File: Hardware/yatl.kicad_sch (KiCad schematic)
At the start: 17 parts

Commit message: Added schematic and update pins definition
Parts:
- removed AD?: 6x1F-H8.5, arduino_Uno_Rev3-02-TH:1X06, symbol arduino_Uno_Rev3-02-TH-eagle-import:PINHD-1X6
- removed C? (x2): 100n, arduino_Uno_Rev3-02-TH:C0603-ROUND, symbol arduino_Uno_Rev3-02-TH-eagle-import:C-EU0603-RND
- removed D?: CD1206-S01575, arduino_Uno_Rev3-02-TH:MINIMELF, symbol arduino_Uno_Rev3-02-TH-eagle-import:DIODE-MINIMELF
- removed ICSP?: 3x2 M, arduino_Uno_Rev3-02-TH:2X03, symbol arduino_Uno_Rev3-02-TH-eagle-import:PINHD-2X3
- removed IOH?: 10x1F-H8.5, arduino_Uno_Rev3-02-TH:1X10, symbol arduino_Uno_Rev3-02-TH-eagle-import:PINHD-1X10_ARD
- removed IOL?: 8x1F-H8.5, arduino_Uno_Rev3-02-TH:1X08, symbol arduino_Uno_Rev3-02-TH-eagle-import:PINHD-1X8
- removed R?: 1M, arduino_Uno_Rev3-02-TH:R0603-ROUND, symbol arduino_Uno_Rev3-02-TH-eagle-import:R-EU_R0603
- removed RESET?: TS42031-160R-TR-7260, arduino_Uno_Rev3-02-TH:TS42, symbol arduino_Uno_Rev3-02-TH-eagle-import:TS42
- removed RN?: 10K, arduino_Uno_Rev3-02-TH:CAY16, symbol arduino_Uno_Rev3-02-TH-eagle-import:4R-NCAY16
- removed RN? (x2): 1K, arduino_Uno_Rev3-02-TH:CAY16, symbol arduino_Uno_Rev3-02-TH-eagle-import:4R-NCAY16
- removed U?: LMV358IDGKR, arduino_Uno_Rev3-02-TH:MSOP08, symbol arduino_Uno_Rev3-02-TH-eagle-import:LMV358?MM
- removed Y?: CSTCE16M0V53-R0 16MHZ, arduino_Uno_Rev3-02-TH:RESONATOR, symbol arduino_Uno_Rev3-02-TH-eagle-import:RESONATORMU
- removed ZU?: ATMEGA328P-PU, arduino_Uno_Rev3-02-TH:DIL28-3, symbol arduino_Uno_Rev3-02-TH-eagle-import:ATMEGA328P-PU
- added C1: 100n, symbol Device:C
- added C2, C3: 100n, Capacitor_SMD:C_1206_3216Metric_Pad1.33x1.80mm_HandSolder, symbol Device:C
- added J1: (no value), symbol Connector:Conn_01x04_Male
- added J2: Conn_01x08_Male, Connector_PinHeader_2.54mm:PinHeader_1x04_P2.54mm_Vertical, symbol Connector:Conn_01x04_Male
- added L2, L3, L4: (no value), symbol Device:LED
- added RN2, RN3: 100, symbol Device:R
- added RN4: (no value), symbol Device:R
- added SW1: (no value), symbol Switch:SW_SPST
- added U1: (no value), symbol Sensor_Temperature:LM35-LP
- added U2: (no value), symbol MCU_Microchip_ATmega:ATmega328-A
- L1: renamed from L?; value YELLOW -> (none); footprint arduino_Uno_Rev3-02-TH:CHIP-LED0805 -> (none); symbol arduino_Uno_Rev3-02-TH-eagle-import:LEDCHIP-LED0805 -> Device:LED
- RN1: renamed from RN?; value 1K -> (none); footprint arduino_Uno_Rev3-02-TH:CAY16 -> (none); symbol arduino_Uno_Rev3-02-TH-eagle-import:4R-NCAY16 -> Device:R
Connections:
- net GND: now also L1.1 (K), C1.2, C2.2, C3.2, J2.1 (Pin_1), L2.1 (K), L3.1 (K), L4.1 (K), SW1.2 (B), U1.2 (GND), U2.21 (GND), U2.3 (GND), U2.5 (GND); no longer L1.C
- net MISO: now also J1.3 (Pin_3), U2.16 (PB4)
- net MOSI: now also J1.2 (Pin_2), U2.15 (PB3)
- net RESET: now also J1.1 (Pin_1), U2.29 (~{RESET}/PC6)
- net SCK: now also RN1.2, J1.4 (Pin_4), U2.17 (PB5)
- net at RN1.1: now also L1.2 (A); no longer L1.A
- removed net L13: RN1.8 (2)
- new net: L2.2 (A), RN2.1
- new net: L3.2 (A), RN3.1
- new net: L4.2 (A), RN4.2
- new net: C3.1, U2.20 (AREF)
- new net LED0: RN2.2, U2.12 (PB0)
- new net LED1: RN3.2, U2.13 (PB1)
- new net LED2: RN4.1, U2.14 (PB2)
- new net RX: J2.3 (Pin_3), U2.30 (PD0)
- new net SWITCH: SW1.1 (A), U2.32 (PD2)
- new net TEMP: U1.1 (OUT), U2.23 (PC0)
- new net TX: J2.4 (Pin_4), U2.31 (PD1)
- new net VCC: C1.1, C2.1, J2.2 (Pin_2), U1.3 (VDD), U2.18 (AVCC), U2.4 (VCC), U2.6 (VCC)
- no-connect marks 0 -> 14
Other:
- note removed: "0"
- note removed: "1"
- note removed: "10"
- note removed: "11"
- note removed: "12"
- note removed: "13"
- note removed: "2"
- note removed: "3"
- note removed: "4"
- note removed: "5"
- note removed: "6"
- note removed: "7"
- note removed: "8"
- note removed: "9"
- note removed: "SCL"
- note removed: "SDA"

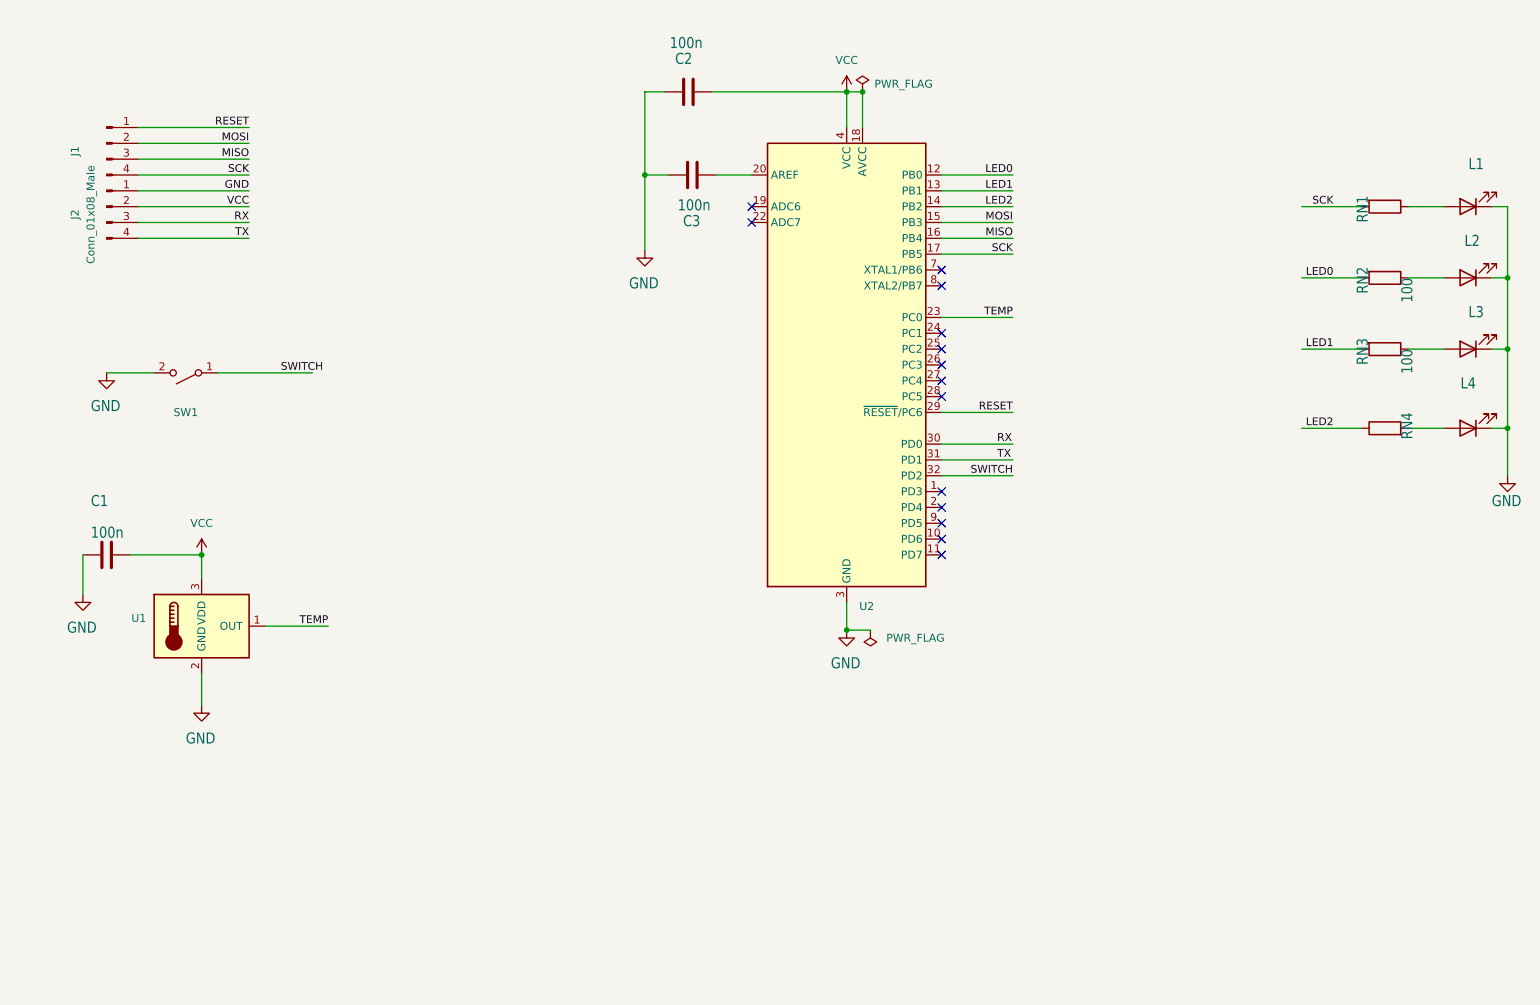
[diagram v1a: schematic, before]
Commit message: Route PCB and update schematics - Add 1x4 testpoint footprint in a project library - Replace LMT86 footprint with 3 1x1 test point - Fix battery decoupling capacitor wiring
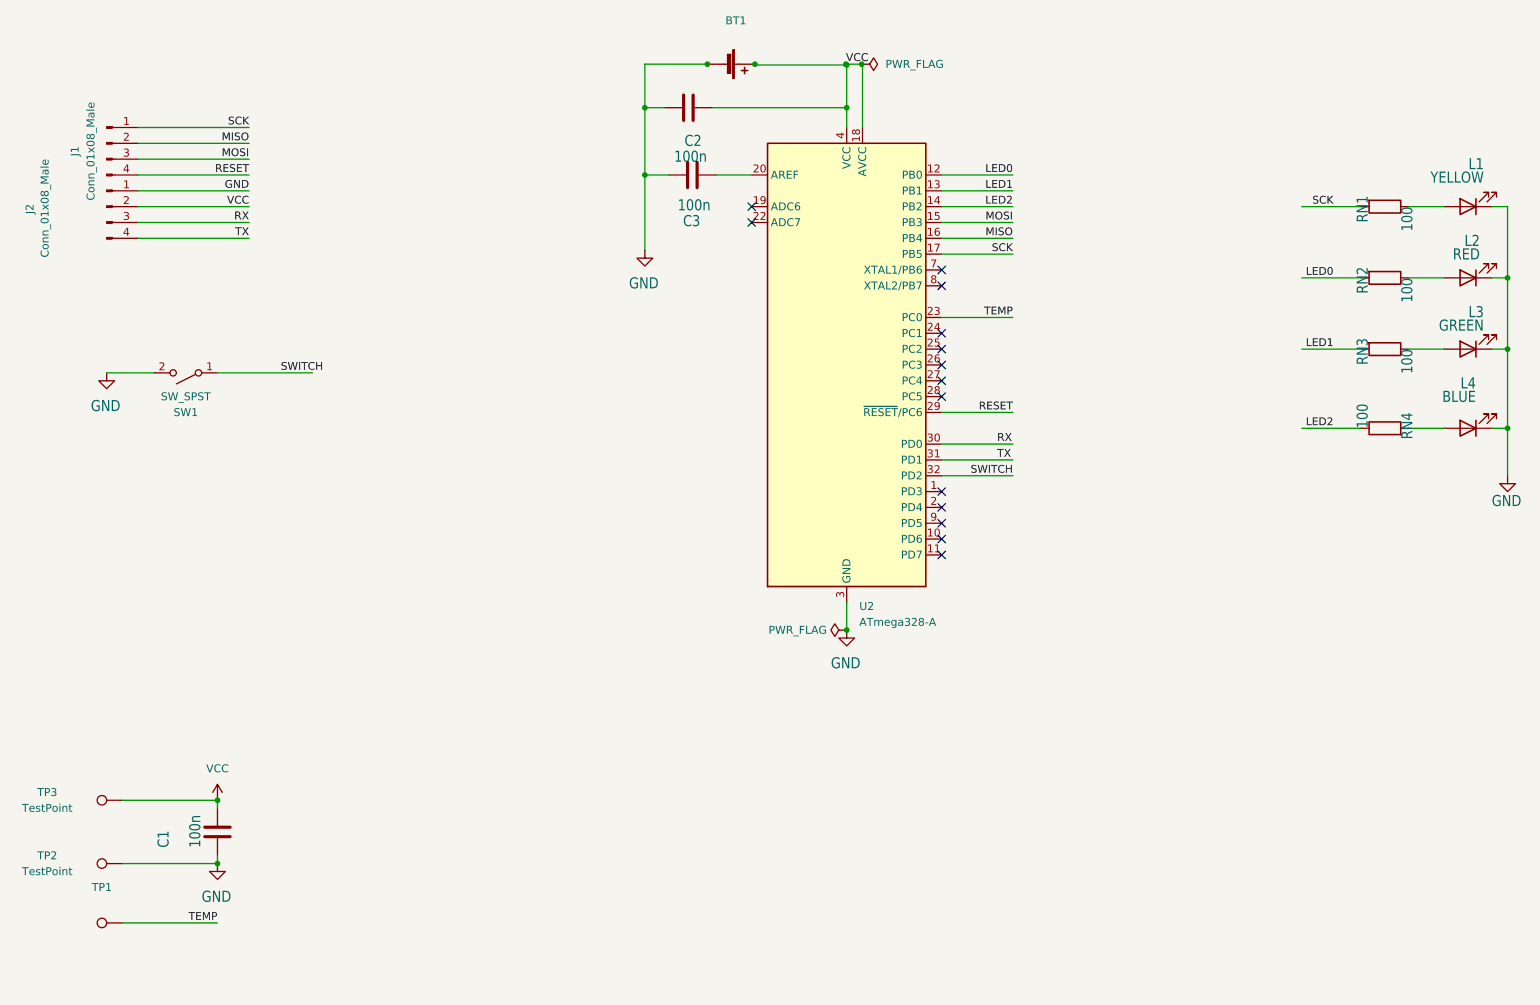
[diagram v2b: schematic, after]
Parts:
- removed U1: (no value), symbol Sensor_Temperature:LM35-LP
- added BT1: (no value), symbol Device:Battery_Cell
- added TP1: (no value), symbol Connector:TestPoint
- added TP2, TP3: TestPoint, symbol Connector:TestPoint
- C1: footprint (none) -> Capacitor_SMD:C_1206_3216Metric_Pad1.33x1.80mm_HandSolder
- J1: value (none) -> Conn_01x08_Male; footprint (none) -> yatl_library:Testpoint_1x04_P2.54mm
- J2: footprint Connector_PinHeader_2.54mm:PinHeader_1x04_P2.54mm_Vertical -> yatl_library:Testpoint_1x04_P2.54mm
- L1: value (none) -> YELLOW; footprint (none) -> LED_SMD:LED_1206_3216Metric_Pad1.42x1.75mm_HandSolder
- L2: value (none) -> RED; footprint (none) -> LED_SMD:LED_1206_3216Metric_Pad1.42x1.75mm_HandSolder
- L3: value (none) -> GREEN; footprint (none) -> LED_SMD:LED_1206_3216Metric_Pad1.42x1.75mm_HandSolder
- L4: value (none) -> BLUE; footprint (none) -> LED_SMD:LED_1206_3216Metric_Pad1.42x1.75mm_HandSolder
- RN1, RN4: value (none) -> 100; footprint (none) -> Resistor_SMD:R_1206_3216Metric_Pad1.30x1.75mm_HandSolder
- RN2, RN3: footprint (none) -> Resistor_SMD:R_1206_3216Metric_Pad1.30x1.75mm_HandSolder
- SW1: value (none) -> SW_SPST; footprint (none) -> Button_Switch_SMD:SW_Push_1P1T_NO_6x6mm_H9.5mm
- U2: value (none) -> ATmega328-A; footprint (none) -> Package_QFP:TQFP-32_7x7mm_P0.8mm
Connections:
- net GND: now also C2.1, BT1.2 (-), TP2.1; no longer C2.2
- net MISO: now also J1.2 (Pin_2); no longer J1.3 (Pin_3)
- net MOSI: now also J1.3 (Pin_3); no longer J1.2 (Pin_2)
- net RESET: now also J1.4 (Pin_4); no longer J1.1 (Pin_1)
- net SCK: now also J1.1 (Pin_1); no longer J1.4 (Pin_4)
- net TEMP: now also TP1.1
- net VCC: now also C2.2, BT1.1 (+), TP3.1; no longer C2.1
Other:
- moved on the sheet: C2

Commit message: Fix pitch between connectors
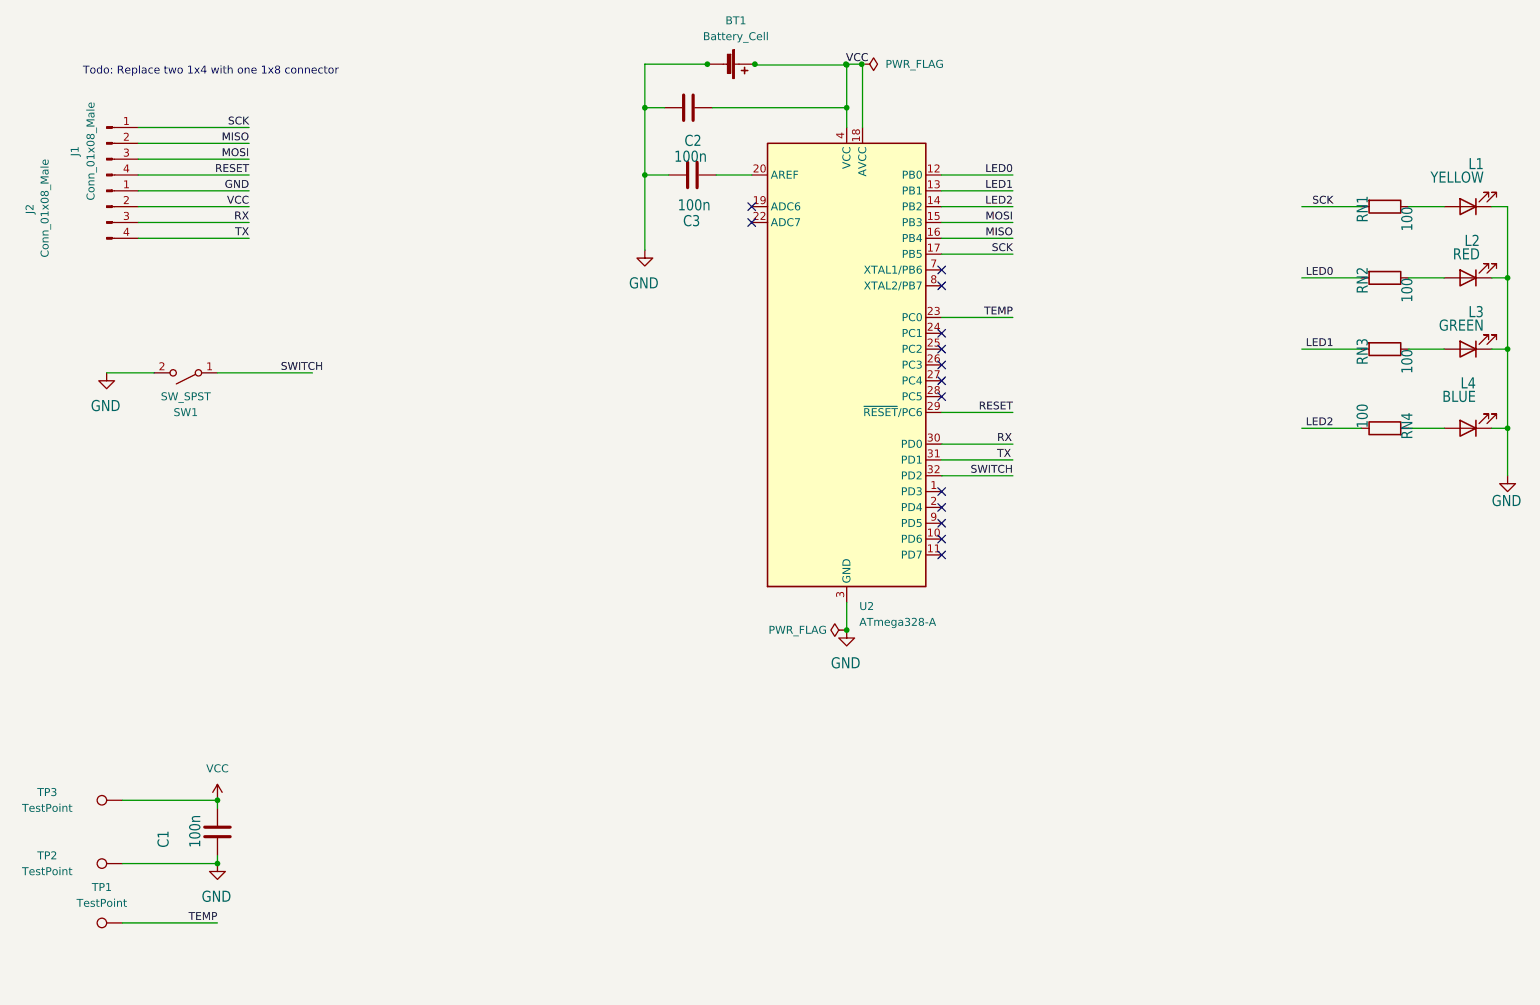
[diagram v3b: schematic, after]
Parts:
- BT1: value (none) -> Battery_Cell; footprint (none) -> Battery:BatteryHolder_Keystone_3034_1x20mm
- TP1: value (none) -> TestPoint; footprint (none) -> TestPoint:TestPoint_Pad_3.0x3.0mm
- TP2, TP3: footprint (none) -> TestPoint:TestPoint_Pad_3.0x3.0mm
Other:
- note added: "Todo: Replace two 1x4 with one 1x8 connector"
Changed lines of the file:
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@@
     (stroke (width 0) (type default) (color 0 0 0 0))
+  )
+  (text "Todo: Replace two 1x4 with one 1x8 connector" (at 40.64 28.575 0)
+    (effects (font (size 1.27 1.27)) (justify left bottom))
   )
   (label "LED2" (at 189.865 49.53 180)
@@
     (in_bom yes) (on_board yes) (fields_autoplaced)
     (property "Reference" "TP1" (id 0) (at 43.688 158.75 90))
-    (property "Value" "" (id 1) (at 43.688 161.29 90))
-    (property "Footprint" "" (id 2) (at 46.99 159.385 0)
+    (property "Value" "TestPoint" (id 1) (at 43.688 161.29 90))
+    (property "Footprint" "TestPoint:TestPoint_Pad_3.0x3.0mm" (id 2) (at 46.99 159.385 0)
       (effects (font (size 1.27 1.27)) hide)
     )
@@
     (property "Reference" "TP3" (id 0) (at 34.925 143.51 90))
     (property "Value" "TestPoint" (id 1) (at 34.925 146.05 90))
-    (property "Footprint" "" (id 2) (at 46.99 139.7 0)
+    (property "Footprint" "TestPoint:TestPoint_Pad_3.0x3.0mm" (id 2) (at 46.99 139.7 0)
       (effects (font (size 1.27 1.27)) hide)
     )
@@
     (in_bom yes) (on_board yes) (fields_autoplaced)
     (property "Reference" "BT1" (id 0) (at 145.415 19.685 90))
-    (property "Value" "" (id 1) (at 145.415 22.225 90))
-    (property "Footprint" "" (id 2) (at 144.907 26.67 90)
+    (property "Value" "Battery_Cell" (id 1) (at 145.415 22.225 90))
+    (property "Footprint" "Battery:BatteryHolder_Keystone_3034_1x20mm" (id 2) (at 144.907 26.67 90)
       (effects (font (size 1.27 1.27)) hide)
     )
@@
     (property "Reference" "TP2" (id 0) (at 34.925 153.67 90))
     (property "Value" "TestPoint" (id 1) (at 34.925 156.21 90))
-    (property "Footprint" "" (id 2) (at 46.99 149.86 0)
-      (effects (font (size 1.27 1.27)) hide)
-    )
+    (property "Footprint" "TestPoint:TestPoint_Pad_3.0x3.0mm" (id 2) (at 46.99 149.86 0)
+      (effects (font (size 1.27 1.27)) hide)
+    )

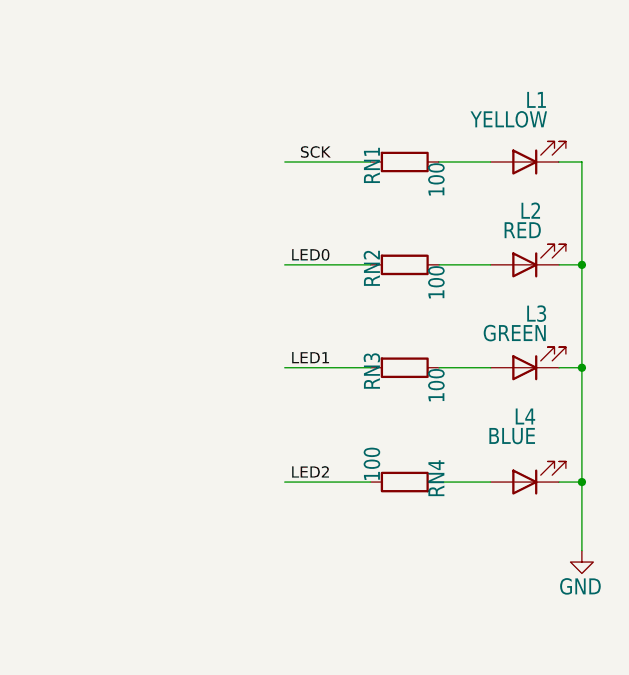
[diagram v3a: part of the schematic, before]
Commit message: Change LED resistor to 2k
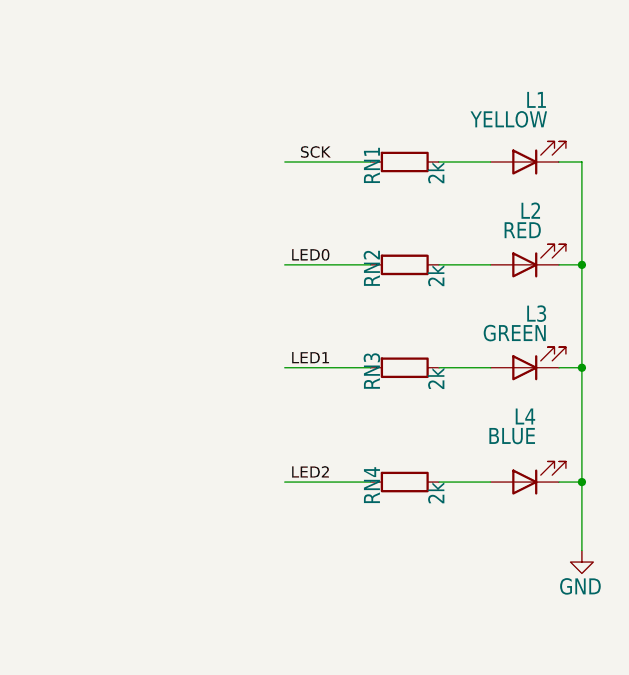
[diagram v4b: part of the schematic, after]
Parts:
- RN1, RN2, RN3, RN4: value 100 -> 2k
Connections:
- net LED2: now also RN4.2; no longer RN4.1
- net at L4.2 (A): now also RN4.1; no longer RN4.2
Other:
- moved on the sheet: RN4
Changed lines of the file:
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@@
       (effects (font (size 1.778 1.5113)) (justify right top))
     )
-    (property "Value" "100" (id 1) (at 252.095 49.53 0)
+    (property "Value" "2k" (id 1) (at 252.095 49.53 0)
       (effects (font (size 1.778 1.5113)) (justify left bottom))
     )
@@
       (effects (font (size 1.778 1.5113)) (justify right top))
     )
-    (property "Value" "100" (id 1) (at 252.095 72.39 0)
+    (property "Value" "2k" (id 1) (at 252.095 72.39 0)
       (effects (font (size 1.778 1.5113)) (justify left bottom))
     )
@@
     (pin "2")
   )
-  (symbol (lib_id "Device:R") (at 249.555 85.09 90) (unit 1)
-    (in_bom yes) (on_board yes)
-    (property "Reference" "RN4" (id 0) (at 252.095 82.55 0)
-      (effects (font (size 1.778 1.5113)) (justify right top))
-    )
-    (property "Value" "100" (id 1) (at 247.015 85.09 0)
-      (effects (font (size 1.778 1.5113)) (justify left bottom))
-    )
-    (property "Footprint" "Resistor_SMD:R_1206_3216Metric_Pad1.30x1.75mm_HandSolder" (id 2) (at 249.555 86.868 90)
+  (symbol (lib_id "Device:R") (at 249.555 85.09 270) (unit 1)
+    (in_bom yes) (on_board yes)
+    (property "Reference" "RN4" (id 0) (at 247.015 87.63 0)
+      (effects (font (size 1.778 1.5113)) (justify right top))
+    )
+    (property "Value" "2k" (id 1) (at 252.095 85.09 0)
+      (effects (font (size 1.778 1.5113)) (justify left bottom))
+    )
+    (property "Footprint" "Resistor_SMD:R_1206_3216Metric_Pad1.30x1.75mm_HandSolder" (id 2) (at 249.555 83.312 90)
       (effects (font (size 1.27 1.27)) hide)
     )
@@
       (effects (font (size 1.778 1.5113)) (justify right top))
     )
-    (property "Value" "100" (id 1) (at 252.095 60.96 0)
+    (property "Value" "2k" (id 1) (at 252.095 60.96 0)
       (effects (font (size 1.778 1.5113)) (justify left bottom))
     )
@@
     )
     (path "/420d34b4-3010-4c28-8f50-a13c623352af"
-      (reference "RN1") (unit 1) (value "100") (footprint "Resistor_SMD:R_1206_3216Metric_Pad1.30x1.75mm_HandSolder")
+      (reference "RN1") (unit 1) (value "2k") (footprint "Resistor_SMD:R_1206_3216Metric_Pad1.30x1.75mm_HandSolder")
     )
     (path "/9b482881-99f9-46bd-af4b-dc2db24183ee"
-      (reference "RN2") (unit 1) (value "100") (footprint "Resistor_SMD:R_1206_3216Metric_Pad1.30x1.75mm_HandSolder")
+      (reference "RN2") (unit 1) (value "2k") (footprint "Resistor_SMD:R_1206_3216Metric_Pad1.30x1.75mm_HandSolder")
     )
     (path "/44dbc5af-18b7-4b4a-9fbe-0fe74ab32e9f"
-      (reference "RN3") (unit 1) (value "100") (footprint "Resistor_SMD:R_1206_3216Metric_Pad1.30x1.75mm_HandSolder")
+      (reference "RN3") (unit 1) (value "2k") (footprint "Resistor_SMD:R_1206_3216Metric_Pad1.30x1.75mm_HandSolder")
     )
     (path "/7ed16553-8d73-4724-bcd1-39d97f91cb58"
-      (reference "RN4") (unit 1) (value "100") (footprint "Resistor_SMD:R_1206_3216Metric_Pad1.30x1.75mm_HandSolder")
+      (reference "RN4") (unit 1) (value "2k") (footprint "Resistor_SMD:R_1206_3216Metric_Pad1.30x1.75mm_HandSolder")
     )
     (path "/7d08da0b-aa56-4fd0-9e56-1760b10fa4de"
